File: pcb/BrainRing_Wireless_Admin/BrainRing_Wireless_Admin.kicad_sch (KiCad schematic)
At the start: 12 parts, among them J1 Butt+WS2812b, Q1 MMBT2222A, U1 LGT8F328P_LQFP32, U2 NRF24L01+PA+LNA, U3 MLT-8530

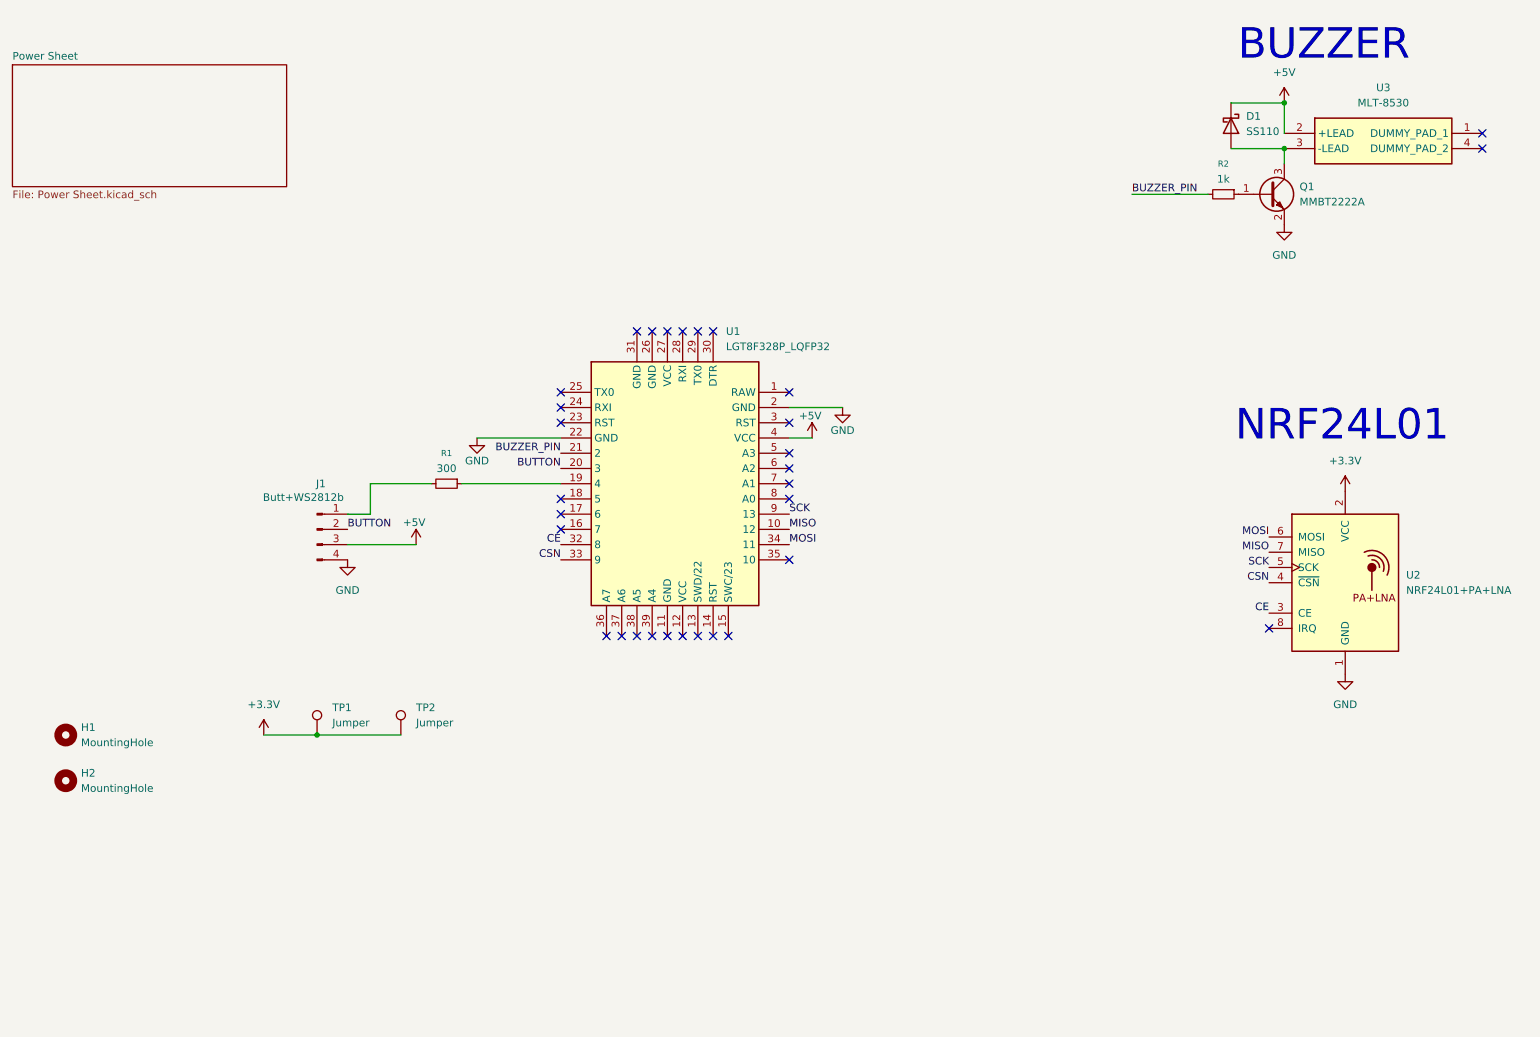
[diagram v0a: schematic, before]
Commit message: Refactor firmware: fair first-press detection, single player firmware, animations
- Shared protocol/radio config (include/brainring.h) and non-blocking melody player (include/melody.h)
- Admin: timestamp-based winner resolution with 30 ms decision window, reject pre-reset presses,
  fresh ACK payloads, press/reset sound and LED indication, idle breathing
- Players: one firmware for all boards, ID/color stored in EEPROM with on-device color menu,
  reliable press delivery with per-ID retry delays, link-loss detection,
  strip + button LED (PWM) animations, 3 random win melodies and a lose melody
- Admin case generator, print files and PCB updates

Co-Authored-By: Claude Opus 5.5 <noreply@anthropic.com>
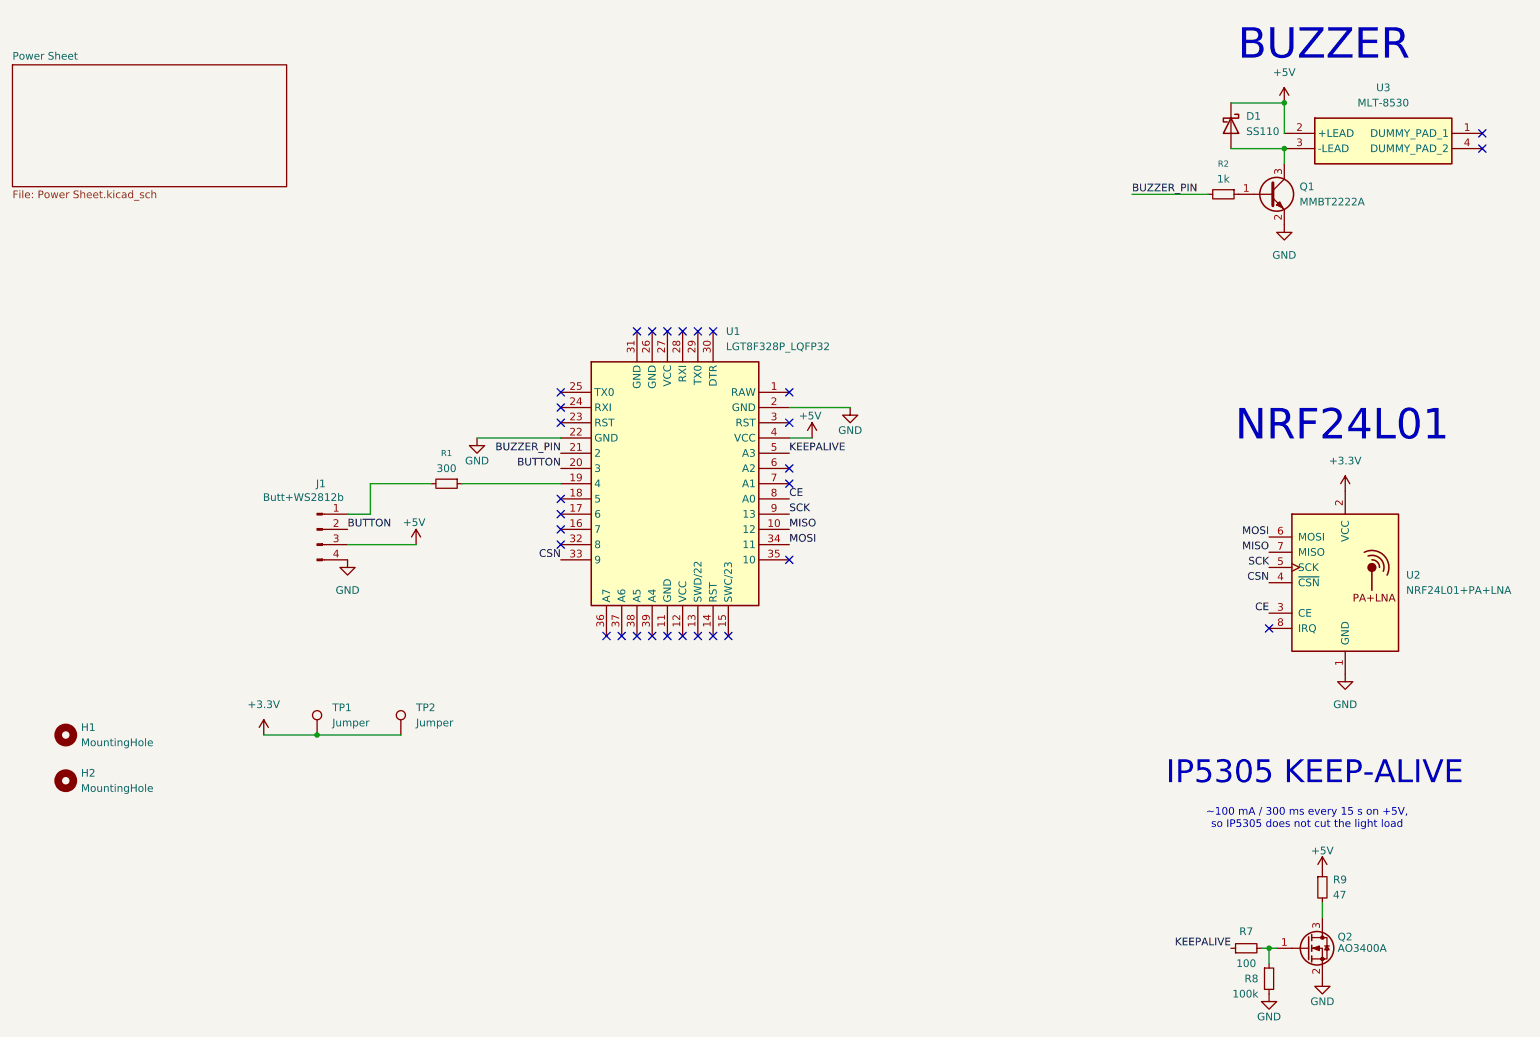
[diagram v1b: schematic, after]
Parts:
- added Q2: AO3400A, Package_TO_SOT_SMD:SOT-23, symbol Transistor_FET:AO3400A
- added R7: 100, Resistor_SMD:R_0603_1608Metric, symbol Device:R_Small
- added R8: 100k, Resistor_SMD:R_0603_1608Metric, symbol Device:R_Small
- added R9: 47, Resistor_SMD:R_1206_3216Metric, symbol Device:R_Small
- H1, H2: footprint MountingHole:MountingHole_2.2mm_M2 -> MountingHole:MountingHole_3.2mm_M3
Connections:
- net +5V: now also R9.1
- net CE: now also U1.8 (A0); no longer U1.32 (8)
- net GND: now also Q2.2 (S), R8.2
- net KEEPALIVE: now reaches U1.5 (A3)
- net KEEPALIVE: now also R7.1
- new net: Q2.1 (G), R7.2, R8.1
- new net: Q2.3 (D), R9.2
- no-connect marks 31 -> 30
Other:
- note added: "IP5305 KEEP-ALIVE"
- note added: "~100 mA / 300 ms every 15 s on +5V, so IP5305 does not cut the light load"
